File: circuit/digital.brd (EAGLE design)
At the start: 56.2 x 50.8 mm, 34 parts, among them IC1 MCP1701-5V, IC2 MCP1700-3.3V, X1 MINI-USB-SCHIELD-32005-301

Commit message: - цифровая схема, которую будем печатать
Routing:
- net N$9: track 0.00 -> 13.3 mm
- added copper zone on layer 16, net GNDA
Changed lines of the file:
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@@
 <grid distance="0.025" unitdist="inch" unit="mm" style="lines" multiple="1" display="no" altdistance="0.05" altunitdist="mm" altunit="mm"/>
 <layers>
-<layer number="1" name="Top" color="4" fill="1" visible="yes" active="yes"/>
+<layer number="1" name="Top" color="4" fill="1" visible="no" active="yes"/>
 <layer number="16" name="Bottom" color="1" fill="1" visible="yes" active="yes"/>
 <layer number="17" name="Pads" color="2" fill="1" visible="yes" active="yes"/>
 <layer number="18" name="Vias" color="2" fill="1" visible="yes" active="yes"/>
-<layer number="19" name="Unrouted" color="6" fill="1" visible="yes" active="yes"/>
+<layer number="19" name="Unrouted" color="6" fill="1" visible="no" active="yes"/>
 <layer number="20" name="Dimension" color="15" fill="1" visible="yes" active="yes"/>
-<layer number="21" name="tPlace" color="7" fill="1" visible="yes" active="yes"/>
-<layer number="22" name="bPlace" color="7" fill="1" visible="yes" active="yes"/>
-<layer number="23" name="tOrigins" color="15" fill="1" visible="yes" active="yes"/>
-<layer number="24" name="bOrigins" color="15" fill="1" visible="yes" active="yes"/>
+<layer number="21" name="tPlace" color="7" fill="1" visible="no" active="yes"/>
+<layer number="22" name="bPlace" color="7" fill="1" visible="no" active="yes"/>
+<layer number="23" name="tOrigins" color="15" fill="1" visible="no" active="yes"/>
+<layer number="24" name="bOrigins" color="15" fill="1" visible="no" active="yes"/>
 <layer number="25" name="tNames" color="7" fill="1" visible="no" active="yes"/>
 <layer number="26" name="bNames" color="7" fill="1" visible="no" active="yes"/>
-<layer number="27" name="tValues" color="7" fill="1" visible="yes" active="yes"/>
-<layer number="28" name="bValues" color="7" fill="1" visible="yes" active="yes"/>
+<layer number="27" name="tValues" color="7" fill="1" visible="no" active="yes"/>
+<layer number="28" name="bValues" color="7" fill="1" visible="no" active="yes"/>
 <layer number="29" name="tStop" color="7" fill="3" visible="no" active="yes"/>
 <layer number="30" name="bStop" color="7" fill="6" visible="no" active="yes"/>
@@
 <layer number="35" name="tGlue" color="7" fill="4" visible="no" active="yes"/>
 <layer number="36" name="bGlue" color="7" fill="5" visible="no" active="yes"/>
-<layer number="37" name="tTest" color="7" fill="1" visible="yes" active="yes"/>
-<layer number="38" name="bTest" color="7" fill="1" visible="yes" active="yes"/>
-<layer number="39" name="tKeepout" color="4" fill="11" visible="yes" active="yes"/>
-<layer number="40" name="bKeepout" color="1" fill="11" visible="yes" active="yes"/>
-<layer number="41" name="tRestrict" color="4" fill="10" visible="yes" active="yes"/>
-<layer number="42" name="bRestrict" color="1" fill="10" visible="yes" active="yes"/>
-<layer number="43" name="vRestrict" color="2" fill="10" visible="yes" active="yes"/>
-<layer number="44" name="Drills" color="7" fill="1" visible="yes" active="yes"/>
-<layer number="45" name="Holes" color="7" fill="1" visible="yes" active="yes"/>
-<layer number="46" name="Milling" color="3" fill="1" visible="yes" active="yes"/>
-<layer number="47" name="Measures" color="7" fill="1" visible="yes" active="yes"/>
-<layer number="48" name="Document" color="7" fill="1" visible="yes" active="yes"/>
-<layer number="49" name="Reference" color="7" fill="1" visible="yes" active="yes"/>
-<layer number="50" name="dxf" color="7" fill="1" visible="yes" active="yes"/>
-<layer number="51" name="tDocu" color="7" fill="1" visible="yes" active="yes"/>
-<layer number="52" name="bDocu" color="7" fill="1" visible="yes" active="yes"/>
+<layer number="37" name="tTest" color="7" fill="1" visible="no" active="yes"/>
+<layer number="38" name="bTest" color="7" fill="1" visible="no" active="yes"/>
+<layer number="39" name="tKeepout" color="4" fill="11" visible="no" active="yes"/>
+<layer number="40" name="bKeepout" color="1" fill="11" visible="no" active="yes"/>
+<layer number="41" name="tRestrict" color="4" fill="10" visible="no" active="yes"/>
+<layer number="42" name="bRestrict" color="1" fill="10" visible="no" active="yes"/>
+<layer number="43" name="vRestrict" color="2" fill="10" visible="no" active="yes"/>
+<layer number="44" name="Drills" color="7" fill="1" visible="no" active="yes"/>
+<layer number="45" name="Holes" color="7" fill="1" visible="no" active="yes"/>
+<layer number="46" name="Milling" color="3" fill="1" visible="no" active="yes"/>
+<layer number="47" name="Measures" color="7" fill="1" visible="no" active="yes"/>
+<layer number="48" name="Document" color="7" fill="1" visible="no" active="yes"/>
+<layer number="49" name="Reference" color="7" fill="1" visible="no" active="yes"/>
+<layer number="50" name="dxf" color="7" fill="1" visible="no" active="yes"/>
+<layer number="51" name="tDocu" color="7" fill="1" visible="no" active="yes"/>
+<layer number="52" name="bDocu" color="7" fill="1" visible="no" active="yes"/>
 <layer number="91" name="Nets" color="2" fill="1" visible="no" active="no"/>
 <layer number="92" name="Busses" color="1" fill="1" visible="no" active="no"/>
@@
 <layer number="98" name="Guide" color="6" fill="1" visible="no" active="no"/>
 <layer number="100" name="Muster" color="7" fill="1" visible="no" active="no"/>
-<layer number="101" name="Patch_Top" color="12" fill="4" visible="yes" active="yes"/>
-<layer number="116" name="Patch_BOT" color="9" fill="4" visible="yes" active="yes"/>
+<layer number="101" name="Patch_Top" color="12" fill="4" visible="no" active="yes"/>
+<layer number="116" name="Patch_BOT" color="9" fill="4" visible="no" active="yes"/>
 <layer number="200" name="200bmp" color="1" fill="10" visible="no" active="no"/>
 <layer number="250" name="Descript" color="3" fill="1" visible="no" active="no"/>
 <layer number="251" name="SMDround" color="12" fill="11" visible="no" active="no"/>
-<layer number="254" name="cooling" color="7" fill="1" visible="yes" active="yes"/>
+<layer number="254" name="cooling" color="7" fill="1" visible="no" active="yes"/>
 </layers>
 <board>
@@
 <wire x1="36.83" y1="38.735" x2="36.83" y2="37.145" width="0.4064" layer="1"/>
 <wire x1="36.83" y1="37.145" x2="37.145" y2="36.83" width="0.4064" layer="1"/>
+<polygon width="0.4064" layer="16" isolate="0.4064">
+<vertex x="0" y="0"/>
+<vertex x="56.515" y="0"/>
+<vertex x="56.515" y="50.8"/>
+<vertex x="0" y="50.8"/>
+</polygon>
 </signal>
 <signal name="V_ADC">
@@
 <wire x1="25.765" y1="32.765" x2="25.765" y2="33.925" width="0.254" layer="1"/>
 <wire x1="25.765" y1="33.925" x2="24.765" y2="34.925" width="0.254" layer="1"/>
-<via x="24.765" y="34.925" extent="1-16" drill="0.6" diameter="1.4224" shape="square"/>
+<via x="24.765" y="34.925" extent="1-16" drill="0.6" diameter="1.4224"/>
 <wire x1="24.765" y1="34.925" x2="24.765" y2="37.785" width="0.4064" layer="16"/>
 <wire x1="51.435" y1="22.225" x2="38.735" y2="22.225" width="0.4064" layer="16"/>
@@
 <wire x1="21.265" y1="32.765" x2="21.265" y2="34.6" width="0.254" layer="1"/>
 <wire x1="21.265" y1="34.6" x2="21.59" y2="34.925" width="0.254" layer="1"/>
-<via x="21.59" y="34.925" extent="1-16" drill="0.6" diameter="1.4224" shape="square"/>
+<via x="21.59" y="34.925" extent="1-16" drill="0.6" diameter="1.4224"/>
 <wire x1="21.59" y1="34.925" x2="21.59" y2="37.785" width="0.4064" layer="16"/>
 <wire x1="51.435" y1="19.685" x2="36.83" y2="19.685" width="0.4064" layer="16"/>
@@
 <wire x1="12.065" y1="20.955" x2="12.065" y2="23.495" width="0.25" layer="1"/>
 <wire x1="12.065" y1="23.495" x2="13.335" y2="23.495" width="0.25" layer="1"/>
-<wire x1="14.605" y1="23.915" x2="13.755" y2="23.495" width="0" layer="19" extent="1-16"/>
 <wire x1="13.335" y1="23.495" x2="14.605" y2="23.915" width="0.25" layer="1"/>
 </signal>
@@
 <wire x1="31.75" y1="48.895" x2="31.75" y2="49.53" width="0.4064" layer="1"/>
 <wire x1="32.815" y1="48.895" x2="31.75" y2="48.895" width="0.4064" layer="1"/>
-<wire x1="2.08" y1="26.04" x2="1.905" y2="26.035" width="0" layer="19" extent="1-1"/>
 </signal>
 <signal name="N$3">
@@
 <wire x1="20.265" y1="40.06" x2="19.685" y2="40.64" width="0.254" layer="1"/>
 </signal>
+<signal name="N$9">
+<wire x1="6.985" y1="0" x2="0" y2="0" width="0.4064" layer="16"/>
+<wire x1="0" y1="0" x2="0" y2="6.35" width="0.4064" layer="16"/>
+</signal>
 </signals>

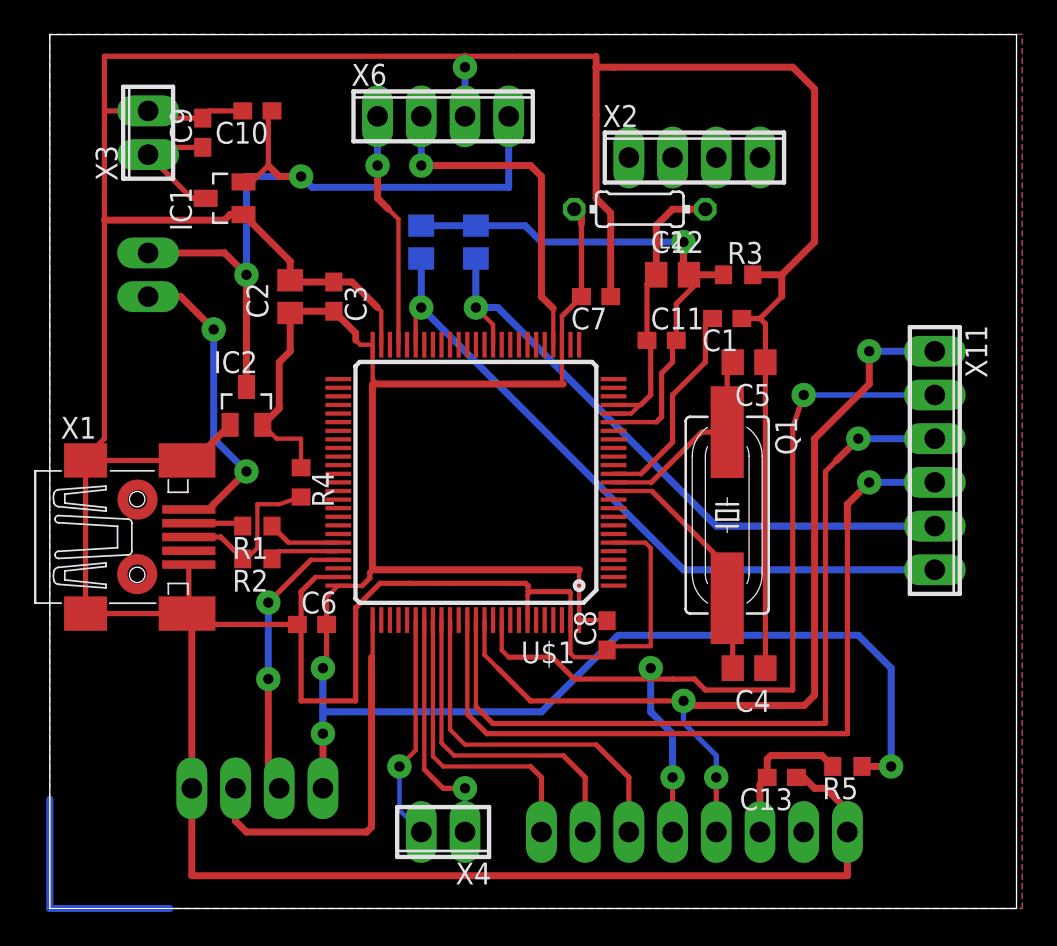
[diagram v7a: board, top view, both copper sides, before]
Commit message: - прикрутили коннектор для энкодера
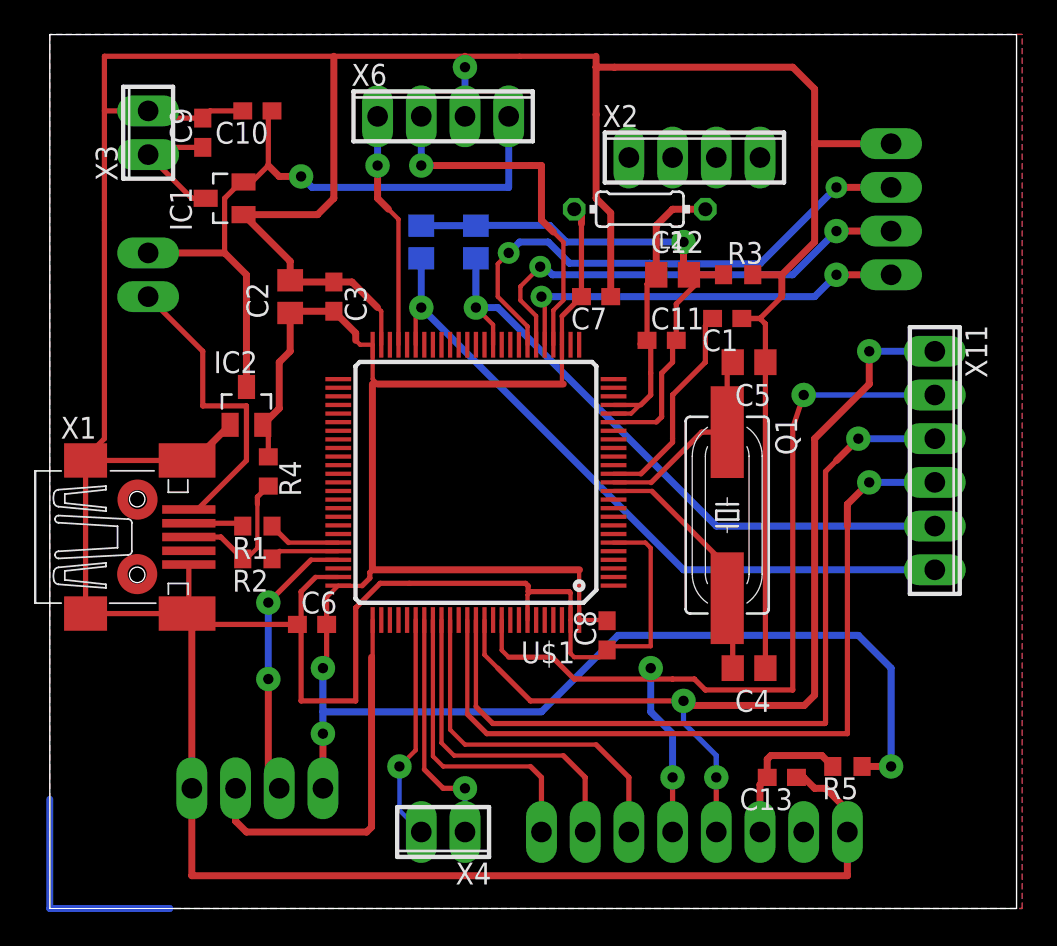
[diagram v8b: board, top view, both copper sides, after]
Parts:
- added X7: (no value), con-phoenix-254:4POL254
- moved R4 2.01 mm to (12.7, 25.4)
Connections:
- new net ENC_A: U$1.31, X7.2
- new net ENC_B: U$1.32, X7.3
- new net ENC_BUTTON: U$1.30, X7.1
- net GND: now also X7.4
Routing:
- net ENC_B: track 0.00 -> 31.2 mm, vias 0 -> 2
- net ENC_A: track 0.00 -> 27.0 mm, vias 0 -> 2
- net ENC_BUTTON: track 0.00 -> 23.7 mm, vias 0 -> 2
- net GND: track 295.5 -> 305.6 mm
- net +5V: track 45.6 -> 41.4 mm, vias 2 -> 1
- net +3V3: track 126.8 -> 124.6 mm
- net N$2: track 9.92 -> 8.63 mm
- net GENERATOR: track 20.2 -> 21.0 mm
- net N$8: vias 2 -> 0
